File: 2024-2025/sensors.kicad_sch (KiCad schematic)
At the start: 15 parts, among them U14 MCP602-E/SN, U15 ADS1115IRUGR, U16 ADS1115IRUGR, U18 LIS3DHTR

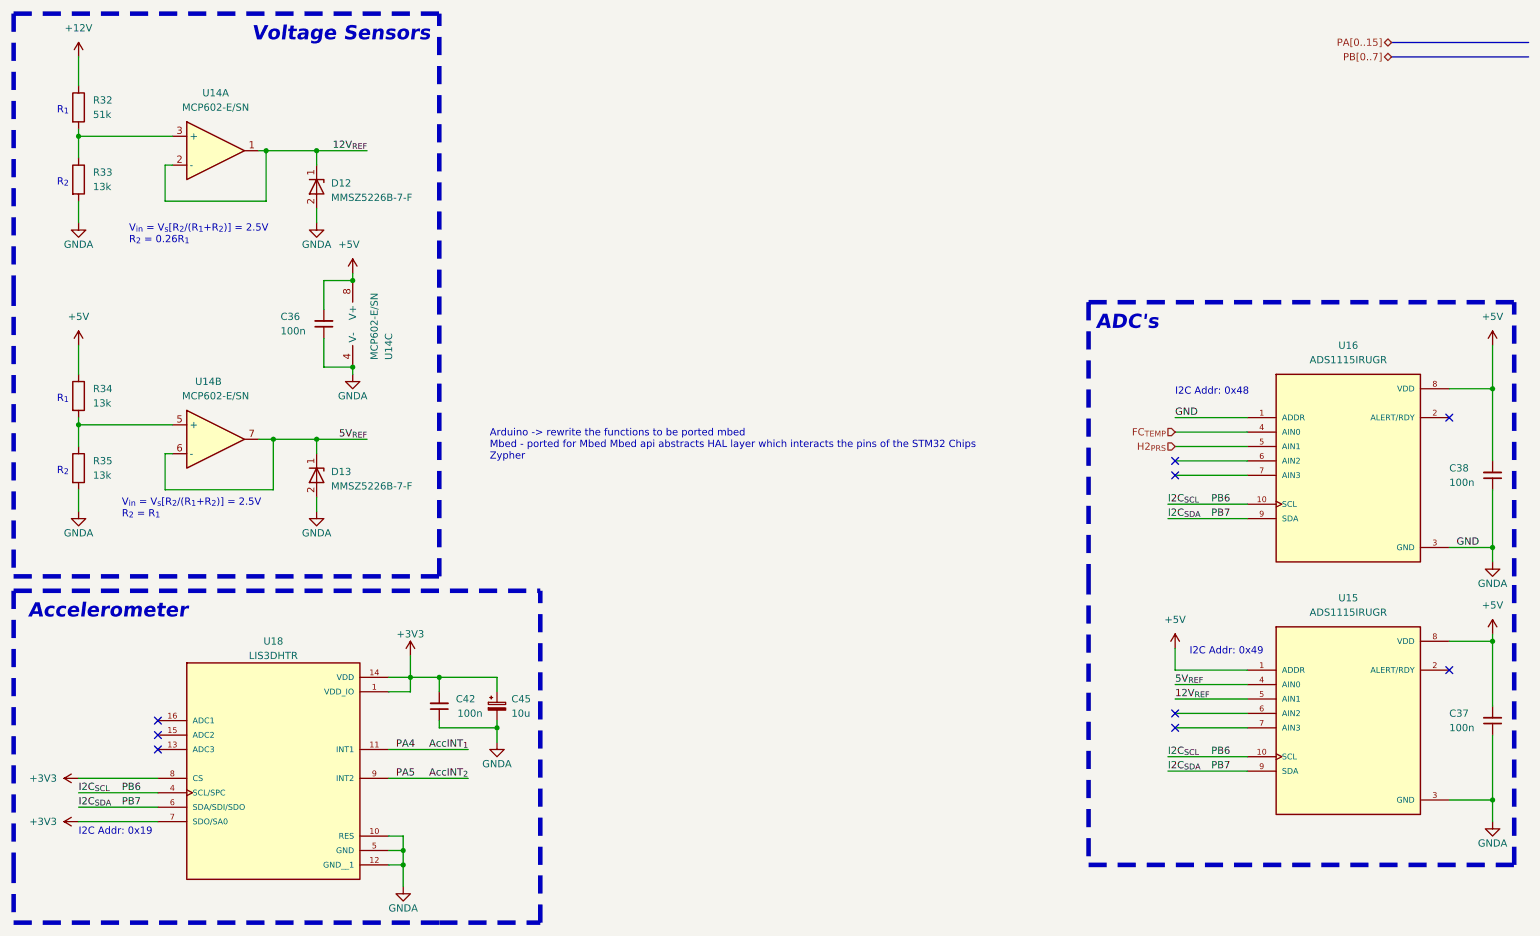
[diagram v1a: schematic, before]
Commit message: MCU 95% retro fit. All old references should be renamed; nets are broken. i.e. labels dont match nets, Peripherals nets dont all match MCU nets.
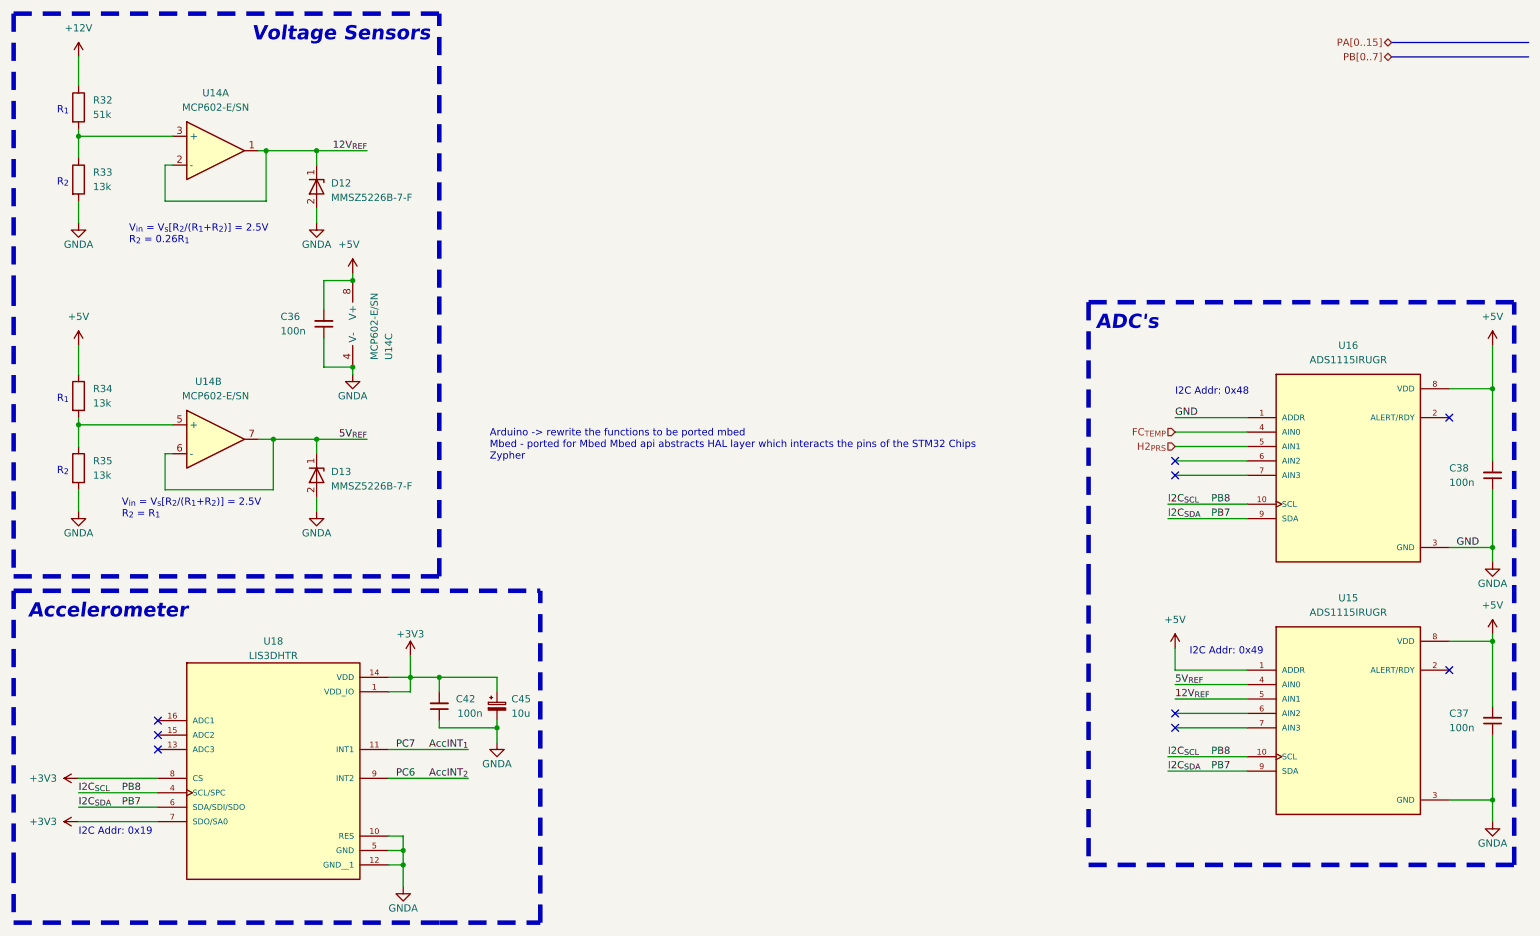
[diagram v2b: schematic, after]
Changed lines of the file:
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@@
 		)
 	)
-	(label "PB6"
+	(label "PB8"
 		(at 224.79 100.33 0)
 		(fields_autoplaced yes)
@@
 		)
 	)
-	(label "PB6"
+	(label "PB8"
 		(at 33.02 151.13 0)
 		(fields_autoplaced yes)
@@
 		)
 	)
-	(label "PA4"
+	(label "PC7"
 		(at 81.28 143.51 0)
 		(fields_autoplaced yes)
@@
 		)
 	)
-	(label "PA5"
+	(label "PC6"
 		(at 81.28 148.59 0)
 		(fields_autoplaced yes)
@@
 		)
 	)
-	(label "PB6"
+	(label "PB8"
 		(at 224.79 144.78 0)
 		(fields_autoplaced yes)

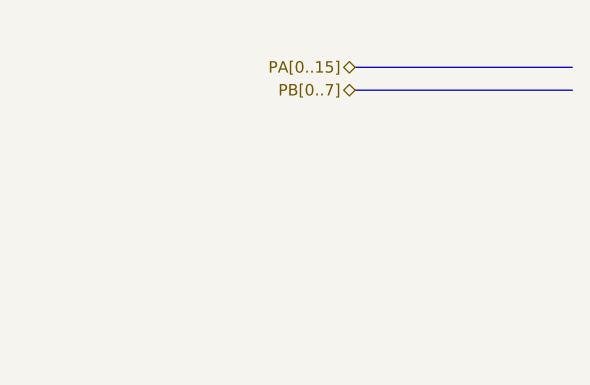
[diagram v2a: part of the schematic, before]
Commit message: basic changes Need to add reset & program header to MCU; replaced CAN connector
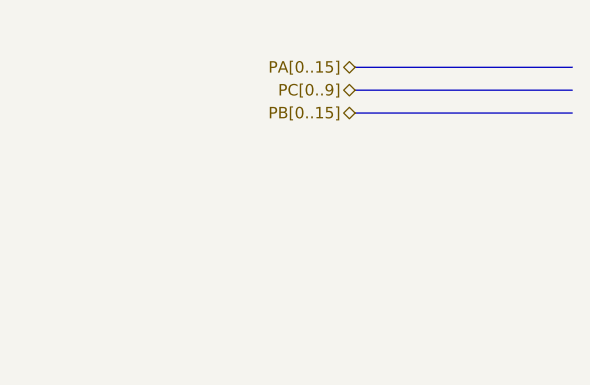
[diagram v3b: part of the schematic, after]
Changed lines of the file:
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@@
+		)
+	)
+	(bus
+		(pts
+			(xy 256.54 24.13) (xy 280.67 24.13)
+		)
+		(stroke
+			(width 0)
+			(type default)
 		)
 	)
@@
 		)
 	)
-	(hierarchical_label "PB[0..7]"
+	(hierarchical_label "PC[0..9]"
 		(shape bidirectional)
 		(at 256.54 21.59 180)
@@
 		(fields_autoplaced yes)
 		(effects
+			(font
+				(size 1.27 1.27)
+			)
+			(justify right)
+		)
+	)
+	(hierarchical_label "PB[0..15]"
+		(shape bidirectional)
+		(at 256.54 24.13 180)
+		(fields_autoplaced yes)
+		(effects

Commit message: schematic done i hope
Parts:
- removed D12, D13: MMSZ5226B-7-F, FC.FTP:D_SOD_123_M, symbol FCC_Parts:MMSZ5226B-7-F
- removed U14: MCP602-E/SN, Package_SO:SOIC-8_3.9x4.9mm_P1.27mm, symbol Device:Opamp_Dual
- removed U15, U16: ADS1115IRUGR, FC.FTP:IC_ADS1115IRUGR, symbol FCC_Parts:ADS1115IRUGR
- removed U18: LIS3DHTR, FC.FTP:XDCR_LIS3DHTR, symbol FCC_Parts:LIS3DHTR
- added D12, D13: MMSZ5226B-7-F, ecocad_lib_footprints:D_SOD_123_M, symbol ecocad_lib_symbols:MMSZ5226B-7-F
- added U12, U15: ADS1115IRUGR, ecocad_lib_footprints:IC_ADS1115IRUGR, symbol ecocad_lib_symbols:ADS1115IRUGR
- added U13: MCP6007, Package_SO:SOIC-8_3.9x4.9mm_P1.27mm, symbol ecocad_lib_symbols:MCP6007
- added U16: LIS3DHTR, ecocad_lib_footprints:XDCR_LIS3DHTR, symbol ecocad_lib_symbols:LIS3DHTR
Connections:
- net +3V3: now also U16.1 (VDD_IO), U16.14 (VDD), U16.7 (SDO/SA0), U16.8 (CS)
- net +5V: now also U12.1 (ADDR), U12.8 (VDD), U13.8 (V+), U15.8 (VDD)
- net 12V_{REF}: now also D12.1, U12.5 (AIN1), U13.1, U13.2 (-)
- net 5V_{REF}: now also D13.1, U12.4 (AIN0), U13.6 (-), U13.7
- net AccINT_{1}: now also U16.11 (INT1)
- net AccINT_{2}: now also U16.9 (INT2)
- net FC_{TEMP}: now also U15.4 (AIN0)
- net GNDA: now also D12.2, D13.2, U12.3 (GND), U13.4 (V-), U15.1 (ADDR), U15.3 (GND), U16.10 (RES), U16.12 (GND__1), U16.5 (GND)
- net H2_{PRS}: now also U15.5 (AIN1)
- net I2C_{SCL}: now also U12.10 (SCL), U15.10 (SCL), U16.4 (SCL/SPC)
- net I2C_{SDA}: now also U12.9 (SDA), U15.9 (SDA), U16.6 (SDA/SDI/SDO)
- net at R34.2, R35.1: now also U13.5 (+)
- net at R32.2, R33.1: now also U13.3 (+)
